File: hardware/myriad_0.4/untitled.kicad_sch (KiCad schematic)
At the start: 15 parts, among them U4 TL074, U5 LM13700

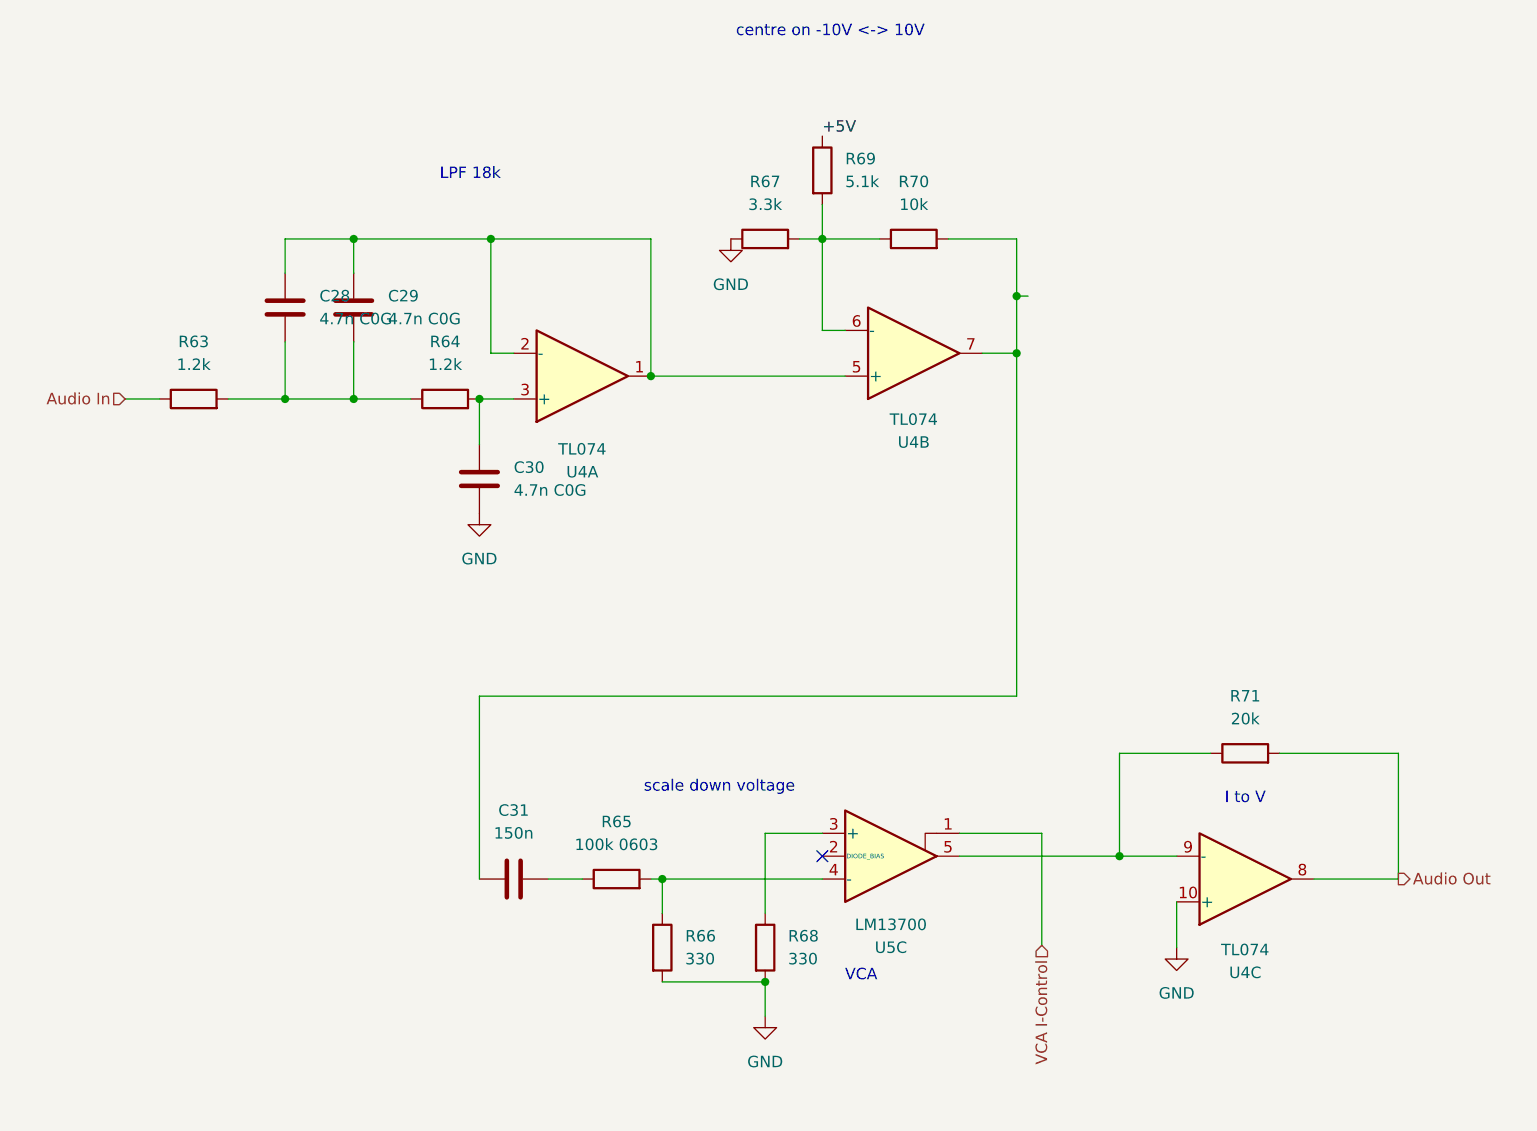
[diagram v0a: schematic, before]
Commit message: separate LR outs
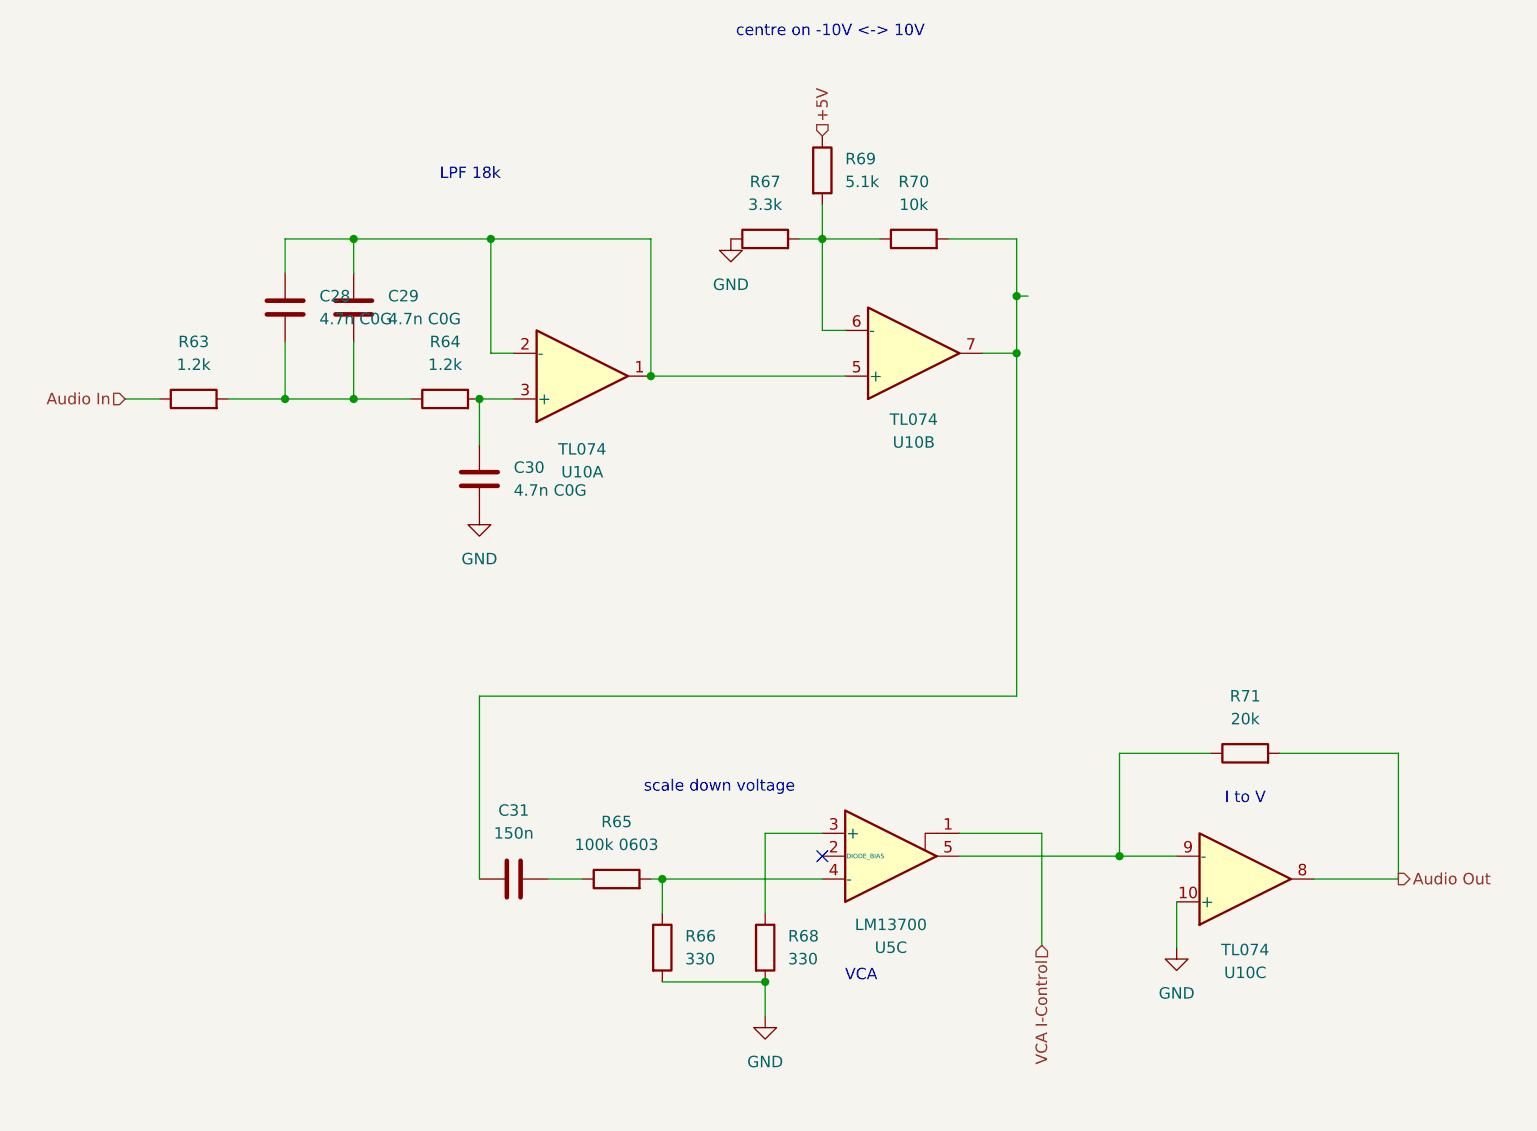
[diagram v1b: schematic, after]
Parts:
- renumbered U4 to U10
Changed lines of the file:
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@@
-		)
-	)
-	(label "+5V"
-		(at 137.033 37.846 0)
-		(effects
-			(font
-				(size 1.27 1.27)
-			)
-			(justify left bottom)
 		)
 	)
@@
 		)
 	)
+	(hierarchical_label "+5V"
+		(shape input)
+		(at 137.033 37.846 90)
+		(effects
+			(font
+				(size 1.27 1.27)
+			)
+			(justify left)
+		)
+	)
 	(symbol
 		(lib_id "power:GND")
@@
 		(on_board yes)
 		(dnp no)
-		(property "Reference" "U4"
+		(property "Reference" "U10"
 			(at 184.023 130.81 0)
 			(effects
@@
 		(on_board yes)
 		(dnp no)
-		(property "Reference" "U4"
+		(property "Reference" "U10"
 			(at 147.193 71.882 0)
 			(effects
@@
 		(on_board yes)
 		(dnp no)
-		(property "Reference" "U4"
+		(property "Reference" "U10"
 			(at 110.363 75.184 0)
 			(effects

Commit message: almost routed
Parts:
- U10: footprint (none) -> Package_SO:TSSOP-14_4.4x5mm_P0.65mm
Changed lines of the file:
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@@
 			)
 		)
-		(property "Footprint" ""
+		(property "Footprint" "Package_SO:TSSOP-14_4.4x5mm_P0.65mm"
 			(at 182.753 122.936 0)
 			(effects
@@
 			)
 		)
-		(property "Footprint" ""
+		(property "Footprint" "Package_SO:TSSOP-14_4.4x5mm_P0.65mm"
 			(at 145.923 64.516 0)
 			(effects
@@
 			)
 		)
-		(property "Footprint" ""
+		(property "Footprint" "Package_SO:TSSOP-14_4.4x5mm_P0.65mm"
 			(at 109.093 67.056 0)
 			(effects

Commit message: tidy up
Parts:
- renumbered C28 to C24, C29 to C25, C30 to C26, C31 to C27, R63 to R54, R64 to R55, R65 to R56, R66 to R57, R67 to R58, R68 to R59, R69 to R60, R70 to R61, R71 to R62, U10 to U4
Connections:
- net VCA I-Control : now also U5.16; no longer U5.1
- net at R62.1, U4.9 (-): now also U5.12; no longer U5.5
- net at R56.2, R57.1: now also U5.13 (-); no longer U5.4 (-)
- net at R59.1: now also U5.14 (+); no longer U5.3 (+)
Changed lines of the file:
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@@
 (kicad_sch
-	(version 20231120)
+	(version 20250114)
 	(generator "eeschema")
-	(generator_version "8.0")
+	(generator_version "9.0")
 	(paper "A4")
+	(text "LPF 18k\n"
+		(exclude_from_sim no)
+		(at 97.917 42.164 0)
+		(effects
+			(font
+				(size 1.27 1.27)
+			)
+		)
+	)
+	(text "I to V"
+		(exclude_from_sim no)
+		(at 184.023 111.506 0)
+		(effects
+			(font
+				(size 1.27 1.27)
+			)
+		)
+	)
+	(text "VCA"
+		(exclude_from_sim no)
+		(at 141.351 131.191 0)
+		(effects
+			(font
+				(size 1.27 1.27)
+			)
+		)
+	)
+	(text "centre on -10V <-> 10V"
+		(exclude_from_sim no)
+		(at 137.922 26.289 0)
+		(effects
+			(font
+				(size 1.27 1.27)
+			)
+		)
+	)
+	(text "scale down voltage"
+		(exclude_from_sim no)
+		(at 125.603 110.236 0)
+		(effects
+			(font
+				(size 1.27 1.27)
+			)
+		)
+	)
 	(junction
 		(at 98.933 67.056)
@@
 			(width 0)
 			(type default)
-		)
-	)
-	(text "LPF 18k\n"
-		(exclude_from_sim no)
-		(at 97.917 42.164 0)
-		(effects
-			(font
-				(size 1.27 1.27)
-			)
-		)
-	)
-	(text "I to V"
-		(exclude_from_sim no)
-		(at 184.023 111.506 0)
-		(effects
-			(font
-				(size 1.27 1.27)
-			)
-		)
-	)
-	(text "VCA"
-		(exclude_from_sim no)
-		(at 141.351 131.191 0)
-		(effects
-			(font
-				(size 1.27 1.27)
-			)
-		)
-	)
-	(text "centre on -10V <-> 10V"
-		(exclude_from_sim no)
-		(at 137.922 26.289 0)
-		(effects
-			(font
-				(size 1.27 1.27)
-			)
-		)
-	)
-	(text "scale down voltage"
-		(exclude_from_sim no)
-		(at 125.603 110.236 0)
-		(effects
-			(font
-				(size 1.27 1.27)
-			)
 		)
 	)
@@
 		(dnp no)
 		(fields_autoplaced yes)
-		(property "Reference" "#PWR091"
+		(property "Reference" "#PWR087"
 			(at 98.933 86.106 0)
 			(effects
@@
 		(dnp no)
 		(fields_autoplaced yes)
-		(property "Reference" "C29"
+		(property "Reference" "C25"
 			(at 88.773 55.6259 0)
 			(effects
@@
 		(on_board yes)
 		(dnp no)
-		(property "Reference" "U10"
+		(property "Reference" "U4"
 			(at 184.023 130.81 0)
 			(effects
@@
 		(dnp no)
 		(fields_autoplaced yes)
-		(property "Reference" "C28"
+		(property "Reference" "C24"
 			(at 81.153 55.6259 0)
 			(effects
@@
 		(dnp no)
 		(fields_autoplaced yes)
-		(property "Reference" "R65"
+		(property "Reference" "R56"
 			(at 114.173 114.046 90)
 			(effects
@@
 		(dnp no)
 		(fields_autoplaced yes)
-		(property "Reference" "R63"
+		(property "Reference" "R54"
 			(at 67.183 60.706 90)
 			(effects
@@
 		(dnp no)
 		(fields_autoplaced yes)
-		(property "Reference" "C31"
+		(property "Reference" "C27"
 			(at 102.743 112.776 90)
 			(effects
@@
 		(dnp no)
 		(fields_autoplaced yes)
-		(property "Reference" "R64"
+		(property "Reference" "R55"
 			(at 95.123 60.706 90)
 			(effects
@@
 		(dnp no)
 		(fields_autoplaced yes)
-		(property "Reference" "R67"
+		(property "Reference" "R58"
 			(at 130.683 42.926 90)
 			(effects
@@
 		(dnp no)
 		(fields_autoplaced yes)
-		(property "Reference" "R71"
+		(property "Reference" "R62"
 			(at 184.023 100.076 90)
 			(effects
@@
 		(dnp no)
 		(fields_autoplaced yes)
-		(property "Reference" "R70"
+		(property "Reference" "R61"
 			(at 147.193 42.926 90)
 			(effects
@@
 		(on_board yes)
 		(dnp no)
-		(property "Reference" "U10"
+		(property "Reference" "U4"
 			(at 147.193 71.882 0)
 			(effects
@@
 		(dnp no)
 		(fields_autoplaced yes)
-		(property "Reference" "#PWR093"
+		(property "Reference" "#PWR089"
 			(at 130.683 141.986 0)
 			(effects
@@
 		(at 144.653 117.856 0)
 		(mirror x)
-		(unit 3)
+		(unit 1)
 		(exclude_from_sim no)
 		(in_bom yes)
@@
 		(dnp no)
 		(fields_autoplaced yes)
-		(property "Reference" "#PWR092"
+		(property "Reference" "#PWR088"
 			(at 126.873 55.626 0)
 			(effects
@@
 		(dnp no)
 		(fields_autoplaced yes)
-		(property "Reference" "R68"
+		(property "Reference" "R59"
 			(at 133.223 126.7459 0)
 			(effects
@@
 		(dnp no)
 		(fields_autoplaced yes)
-		(property "Reference" "R66"
+		(property "Reference" "R57"
 			(at 121.793 126.7459 0)
 			(effects
@@
 		(dnp no)
 		(fields_autoplaced yes)
-		(property "Reference" "C30"
+		(property "Reference" "C26"
 			(at 102.743 74.6759 0)
 			(effects
@@
 		(on_board yes)
 		(dnp no)
-		(property "Reference" "U10"
+		(property "Reference" "U4"
 			(at 110.363 75.184 0)
 			(effects
@@
 		(dnp no)
 		(fields_autoplaced yes)
-		(property "Reference" "#PWR094"
+		(property "Reference" "#PWR090"
 			(at 176.403 134.366 0)
 			(effects
@@
 		(dnp no)
 		(fields_autoplaced yes)
-		(property "Reference" "R69"
+		(property "Reference" "R60"
 			(at 139.573 40.3859 0)
 			(effects
